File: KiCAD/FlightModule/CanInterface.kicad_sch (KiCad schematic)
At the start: 14 parts, among them U8 MCP2562-E-SN, U9 MCP2515-xST, Y1 8MHz

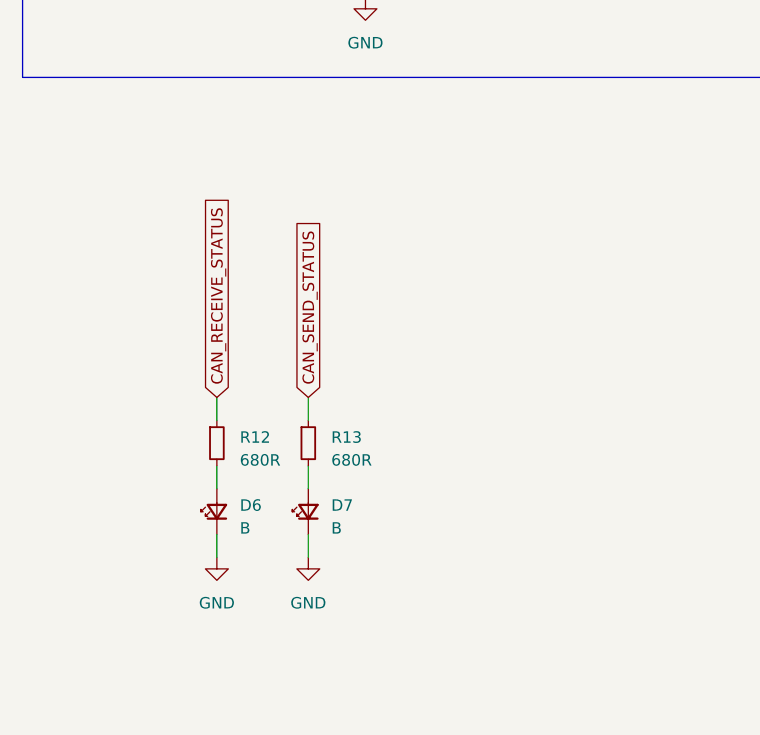
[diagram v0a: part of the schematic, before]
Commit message: バスの回路図完成，LEDの配置を変更
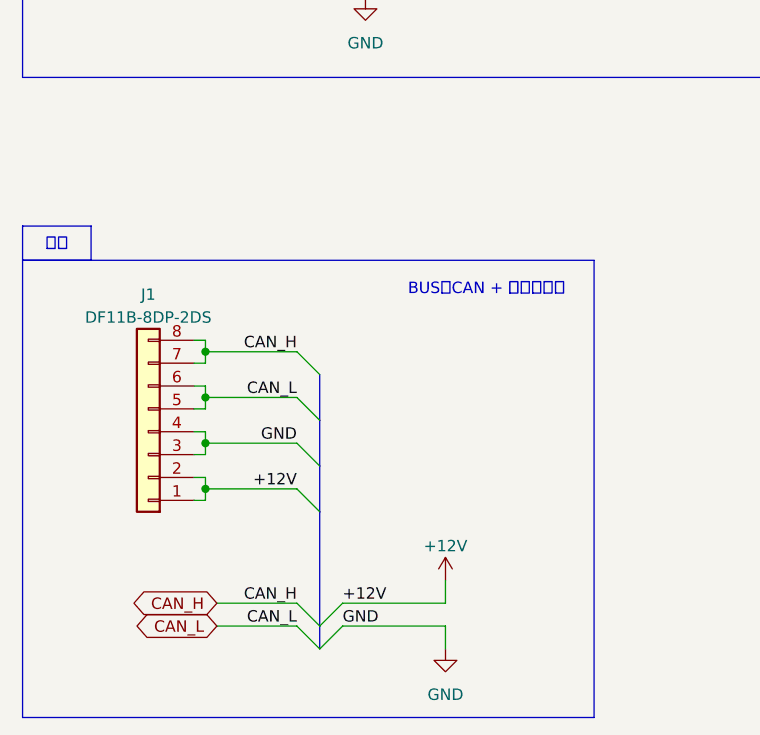
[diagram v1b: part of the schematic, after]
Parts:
- removed D6, D7: B, LED_SMD:LED_0603_1608Metric_Pad1.05x0.95mm_HandSolder, symbol Device:LED_Small
- removed R12, R13: 680R, Resistor_SMD:R_0603_1608Metric_Pad0.98x0.95mm_HandSolder, symbol Device:R_Small
- added J1: DF11B-8DP-2DS, Hirose_Connector:Hirose_DF11B-8DP-2DS, symbol Connector_Generic:Conn_01x08
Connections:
- net CAN_H: now also J1.7 (Pin_7), J1.8 (Pin_8)
- net CAN_L: now also J1.5 (Pin_5), J1.6 (Pin_6)
- net GND: now also J1.3 (Pin_3), J1.4 (Pin_4)
- new net +12V: J1.1 (Pin_1), J1.2 (Pin_2)
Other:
- note added: "BUS：CAN + 電源ライン"

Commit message: 配線8割り終わり．次の作業....
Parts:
- J1: footprint Hirose_Connector:Hirose_DF11B-8DP-2DS -> TSRP_Connector_Hirose:DF11-8DP-2DS
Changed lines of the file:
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@@
 			)
 		)
-		(property "Footprint" "Hirose_Connector:Hirose_DF11B-8DP-2DS"
+		(property "Footprint" "TSRP_Connector_Hirose:DF11-8DP-2DS"
 			(at 39.37 120.65 0)
 			(effects
